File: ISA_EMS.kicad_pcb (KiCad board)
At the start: 2 copper layers, 176.5 x 102.9 mm, 57 parts, among them J1 ISA BUS, J2 EMS Address, J3 ROM Config, U1 74HCT688, U10 74HCT32, U11 74HCT04, U12 74ACT245, U13 AS6C4008-55PCN, U14 AS6C4008-55PCN, U15 AS6C4008-55PCN, U16 AS6C4008-55PCN, U17 74HCT138, U18 74LS573, U19 74LS573, U2 SST39SF040, U20 74LS573, U21 74LS573, U3 AS6C4008-55PCN, U4 AS6C4008-55PCN, U5 AS6C4008-55PCN, U6 AS6C4008-55PCN, U7 74HCT688, U8 74HCT688, U9 74HCT139

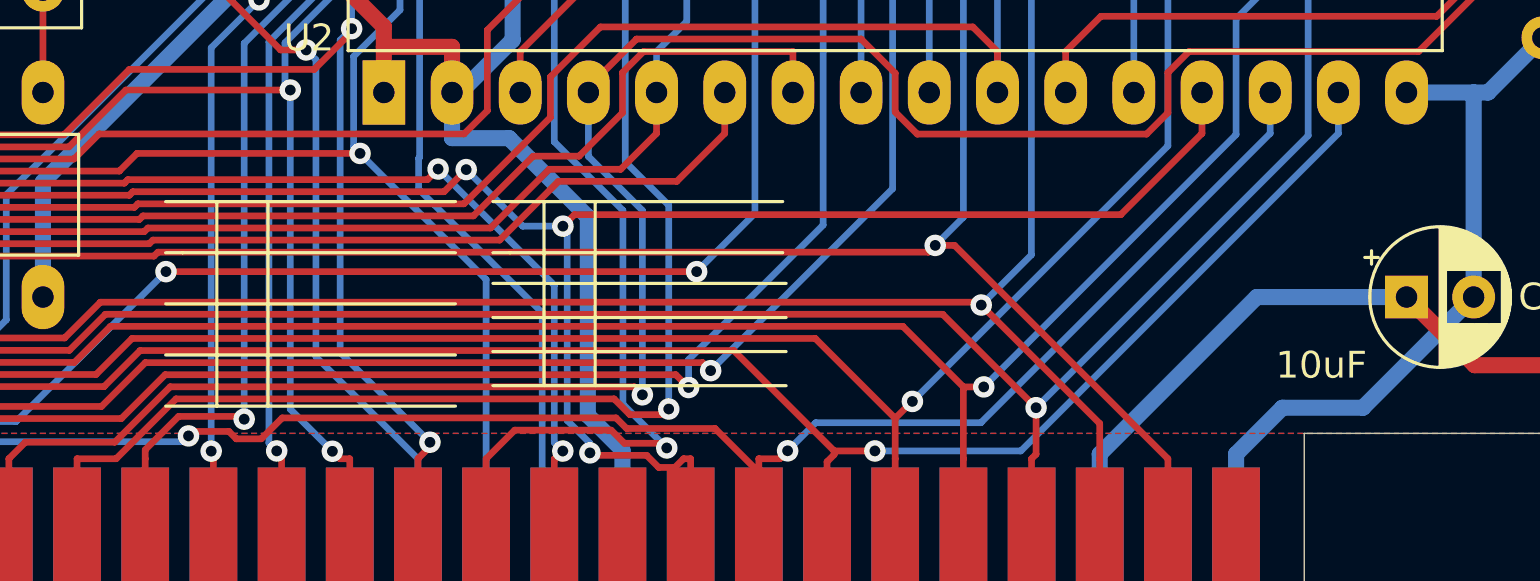
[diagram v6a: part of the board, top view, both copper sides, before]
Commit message: Updated silkscreen
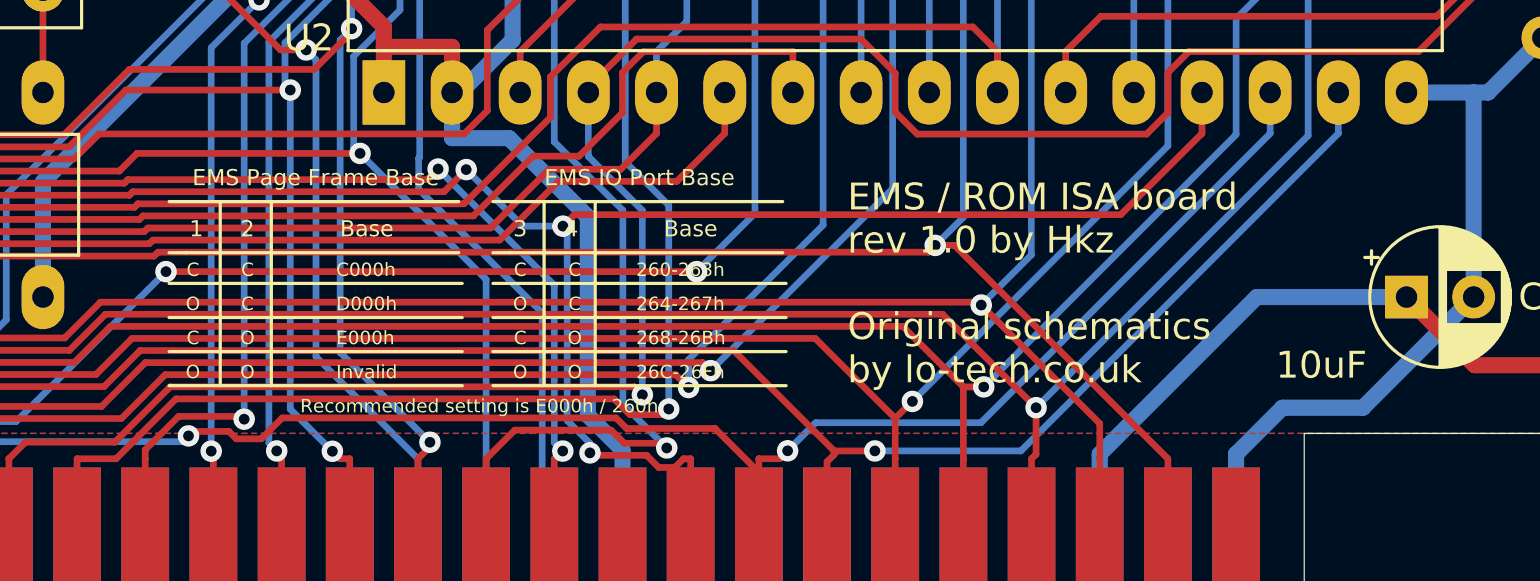
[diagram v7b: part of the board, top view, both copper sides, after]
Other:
- board text added: "260-263h"
- board text added: "264-267h"
- board text added: "268-26Bh"
- board text added: "26C-26Fh"
- board text added: "Base"
- board text added: "C"
- board text added: "C000h"
- board text added: "D000h"
- board text added: "E000h"
- board text added: "EMS / ROM ISA board rev 1.0 by Hkz Original schematics by lo-tech.co.uk"
- board text added: "EMS IO Port Base"
- board text added: "EMS Page Frame Base"
- board text added: "Invalid"
- board text added: "O"
- board text added: "Recommended setting is E000h / 260h"
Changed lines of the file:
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@@
   (general
     (thickness 1.6)
-    (drawings 92)
+    (drawings 127)
     (tracks 3500)
     (zones 0)
@@
     )
   )
+  (gr_text "EMS / ROM ISA board\nrev 1.0 by Hkz\n\nOriginal schematics \nby lo-tech.co.uk" (at 275.082 188.722) (layer F.SilkS)
+    (effects (font (size 1 1) (thickness 0.25)) (justify left))
+  )
+  (gr_text "Recommended setting is E000h / 260h" (at 261.366 193.294) (layer F.SilkS)
+    (effects (font (size 0.5 0.5) (thickness 0.125)))
+  )
+  (gr_text 26C-26Fh (at 267.208 192.024) (layer F.SilkS)
+    (effects (font (size 0.5 0.5) (thickness 0.125)) (justify left))
+  )
+  (gr_text 268-26Bh (at 267.208 190.754) (layer F.SilkS)
+    (effects (font (size 0.5 0.5) (thickness 0.125)) (justify left))
+  )
+  (gr_text 264-267h (at 267.208 189.484) (layer F.SilkS)
+    (effects (font (size 0.5 0.5) (thickness 0.125)) (justify left))
+  )
+  (gr_text 260-263h (at 267.208 188.214) (layer F.SilkS)
+    (effects (font (size 0.5 0.5) (thickness 0.125)) (justify left))
+  )
+  (gr_text O (at 264.922 192.024) (layer F.SilkS)
+    (effects (font (size 0.5 0.5) (thickness 0.125)))
+  )
+  (gr_text C (at 264.922 188.214) (layer F.SilkS)
+    (effects (font (size 0.5 0.5) (thickness 0.125)))
+  )
+  (gr_text C (at 264.922 189.484) (layer F.SilkS)
+    (effects (font (size 0.5 0.5) (thickness 0.125)))
+  )
+  (gr_text C (at 262.89 190.754) (layer F.SilkS)
+    (effects (font (size 0.5 0.5) (thickness 0.125)))
+  )
+  (gr_text O (at 262.89 189.484) (layer F.SilkS)
+    (effects (font (size 0.5 0.5) (thickness 0.125)))
+  )
+  (gr_text O (at 262.89 192.024) (layer F.SilkS)
+    (effects (font (size 0.5 0.5) (thickness 0.125)))
+  )
+  (gr_text O (at 264.922 190.754) (layer F.SilkS)
+    (effects (font (size 0.5 0.5) (thickness 0.125)))
+  )
+  (gr_text C (at 262.89 188.214) (layer F.SilkS)
+    (effects (font (size 0.5 0.5) (thickness 0.125)))
+  )
+  (gr_text C000h (at 256.032 188.214) (layer F.SilkS)
+    (effects (font (size 0.5 0.5) (thickness 0.125)) (justify left))
+  )
+  (gr_text D000h (at 256.032 189.484) (layer F.SilkS)
+    (effects (font (size 0.5 0.5) (thickness 0.125)) (justify left))
+  )
+  (gr_text E000h (at 256.032 190.754) (layer F.SilkS)
+    (effects (font (size 0.5 0.5) (thickness 0.125)) (justify left))
+  )
+  (gr_text Invalid (at 256.032 192.024) (layer F.SilkS)
+    (effects (font (size 0.5 0.5) (thickness 0.125)) (justify left))
+  )
+  (gr_text O (at 252.73 192.024) (layer F.SilkS)
+    (effects (font (size 0.5 0.5) (thickness 0.125)))
+  )
+  (gr_text O (at 250.698 192.024) (layer F.SilkS)
+    (effects (font (size 0.5 0.5) (thickness 0.125)))
+  )
+  (gr_text C (at 250.698 190.754) (layer F.SilkS)
+    (effects (font (size 0.5 0.5) (thickness 0.125)))
+  )
+  (gr_text O (at 252.73 190.754) (layer F.SilkS)
+    (effects (font (size 0.5 0.5) (thickness 0.125)))
+  )
+  (gr_text C (at 252.73 189.484) (layer F.SilkS)
+    (effects (font (size 0.5 0.5) (thickness 0.125)))
+  )
+  (gr_text O (at 250.698 189.484) (layer F.SilkS)
+    (effects (font (size 0.5 0.5) (thickness 0.125)))
+  )
+  (gr_text C (at 252.73 188.214) (layer F.SilkS)
+    (effects (font (size 0.5 0.5) (thickness 0.125)))
+  )
+  (gr_text C (at 250.698 188.214) (layer F.SilkS)
+    (effects (font (size 0.5 0.5) (thickness 0.125)))
+  )
+  (gr_text Base (at 269.24 186.69) (layer F.SilkS)
+    (effects (font (size 0.6 0.6) (thickness 0.15)))
+  )
+  (gr_text Base (at 257.175 186.69) (layer F.SilkS)
+    (effects (font (size 0.6 0.6) (thickness 0.15)))
+  )
+  (gr_text 4 (at 264.795 186.69) (layer F.SilkS)
+    (effects (font (size 0.6 0.6) (thickness 0.15)))
+  )
+  (gr_text 3 (at 262.89 186.69) (layer F.SilkS)
+    (effects (font (size 0.6 0.6) (thickness 0.15)))
+  )
+  (gr_text 2 (at 252.73 186.69) (layer F.SilkS)
+    (effects (font (size 0.6 0.6) (thickness 0.15)))
+  )
+  (gr_text 1 (at 250.825 186.69) (layer F.SilkS)
+    (effects (font (size 0.6 0.6) (thickness 0.15)))
+  )
+  (gr_text "EMS IO Port Base" (at 267.335 184.785) (layer F.SilkS)
+    (effects (font (size 0.6 0.6) (thickness 0.15)))
+  )
+  (gr_text "EMS Page Frame Base" (at 255.27 184.785) (layer F.SilkS)
+    (effects (font (size 0.6 0.6) (thickness 0.15)))
+  )
+  (gr_line (start 250.444 185.674) (end 260.604 185.674) (layer F.SilkS) (width 0.12))
+  (gr_line (start 250.444 185.674) (end 249.809 185.674) (layer F.SilkS) (width 0.12))
+  (gr_line (start 250.444 187.579) (end 249.809 187.579) (layer F.SilkS) (width 0.12))
+  (gr_line (start 250.444 187.579) (end 260.604 187.579) (layer F.SilkS) (width 0.12))
+  (gr_line (start 253.619 187.579) (end 253.619 192.532) (layer F.SilkS) (width 0.12))
+  (gr_line (start 251.714 187.579) (end 251.714 192.532) (layer F.SilkS) (width 0.12))
+  (gr_line (start 249.809 188.722) (end 260.731 188.722) (layer F.SilkS) (width 0.12))
+  (gr_line (start 253.619 185.674) (end 253.619 187.579) (layer F.SilkS) (width 0.12))
+  (gr_line (start 251.714 185.674) (end 251.714 187.579) (layer F.SilkS) (width 0.12))
+  (gr_line (start 249.809 191.262) (end 260.731 191.262) (layer F.SilkS) (width 0.12))
+  (gr_line (start 249.809 192.532) (end 260.731 192.532) (layer F.SilkS) (width 0.12))
+  (gr_line (start 249.809 189.992) (end 260.731 189.992) (layer F.SilkS) (width 0.12))
   (gr_text A15 (at 298.45 163.195 90) (layer F.SilkS)
     (effects (font (size 1 1) (thickness 0.25)))
@@
   (gr_line (start 262.509 185.674) (end 272.669 185.674) (layer F.SilkS) (width 0.12))
   (gr_line (start 263.779 187.579) (end 263.779 192.532) (layer F.SilkS) (width 0.12))
-  (gr_line (start 251.587 187.579) (end 251.587 193.294) (layer F.SilkS) (width 0.12))
-  (gr_line (start 253.492 187.579) (end 253.492 193.294) (layer F.SilkS) (width 0.12))
-  (gr_line (start 249.682 193.294) (end 260.477 193.294) (layer F.SilkS) (width 0.12))
-  (gr_line (start 249.682 191.389) (end 260.477 191.389) (layer F.SilkS) (width 0.12))
-  (gr_line (start 249.682 189.484) (end 260.477 189.484) (layer F.SilkS) (width 0.12))
-  (gr_line (start 253.492 185.674) (end 253.492 187.579) (layer F.SilkS) (width 0.12))
-  (gr_line (start 250.317 187.579) (end 249.682 187.579) (layer F.SilkS) (width 0.12))
-  (gr_line (start 250.317 185.674) (end 249.682 185.674) (layer F.SilkS) (width 0.12))
-  (gr_line (start 251.587 185.674) (end 251.587 187.579) (layer F.SilkS) (width 0.12))
-  (gr_line (start 250.317 187.579) (end 260.477 187.579) (layer F.SilkS) (width 0.12))
-  (gr_line (start 250.317 185.674) (end 260.477 185.674) (layer F.SilkS) (width 0.12))
   (dimension 56.515 (width 0.15) (layer Dwgs.User)
     (gr_text "56,515 mm" (at 328.833 162.8775 90) (layer Dwgs.User)

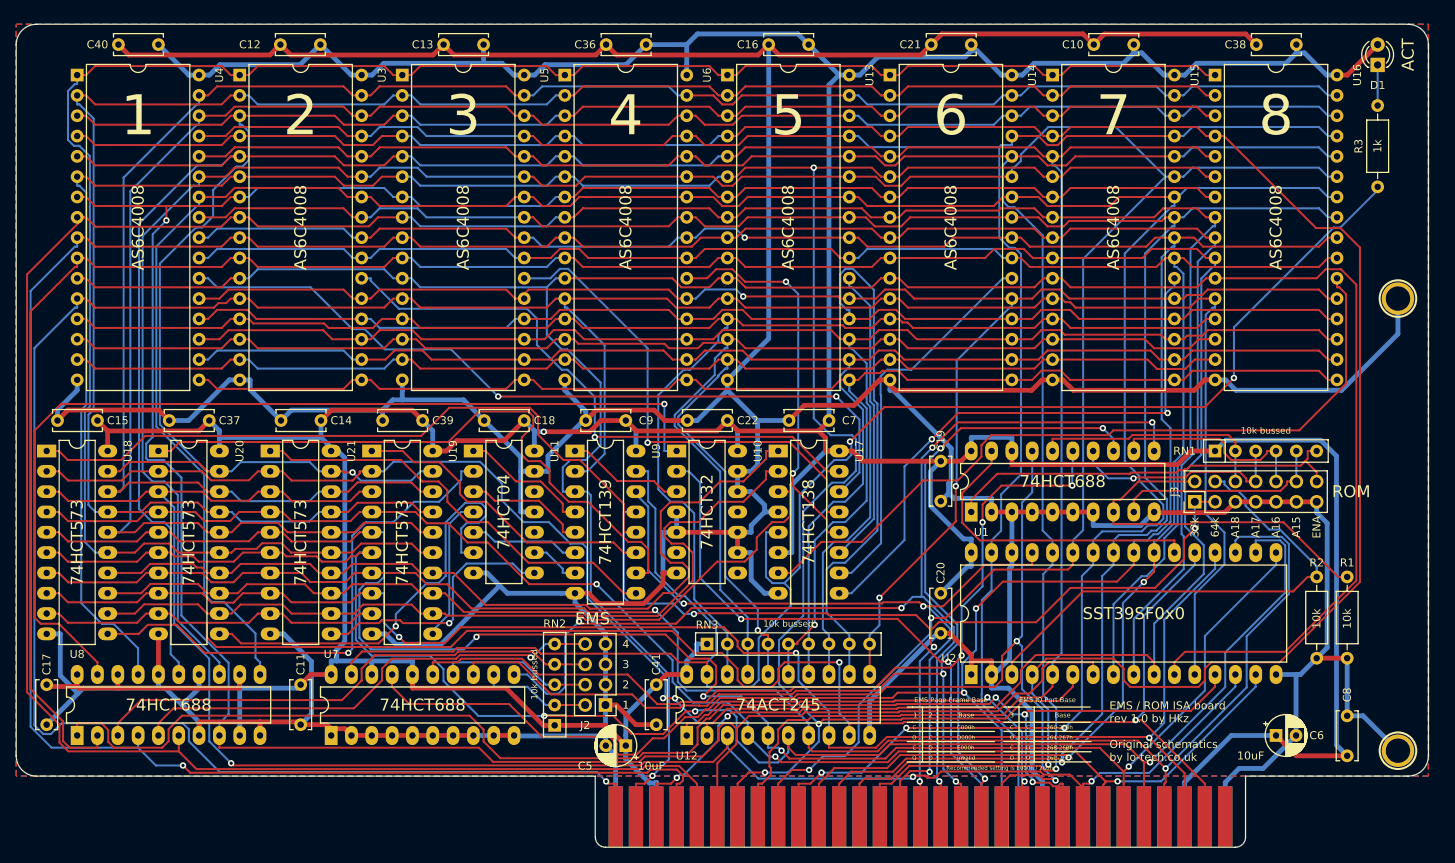
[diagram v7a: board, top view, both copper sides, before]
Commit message: Removed BOOTROM, make board smaller, reroute
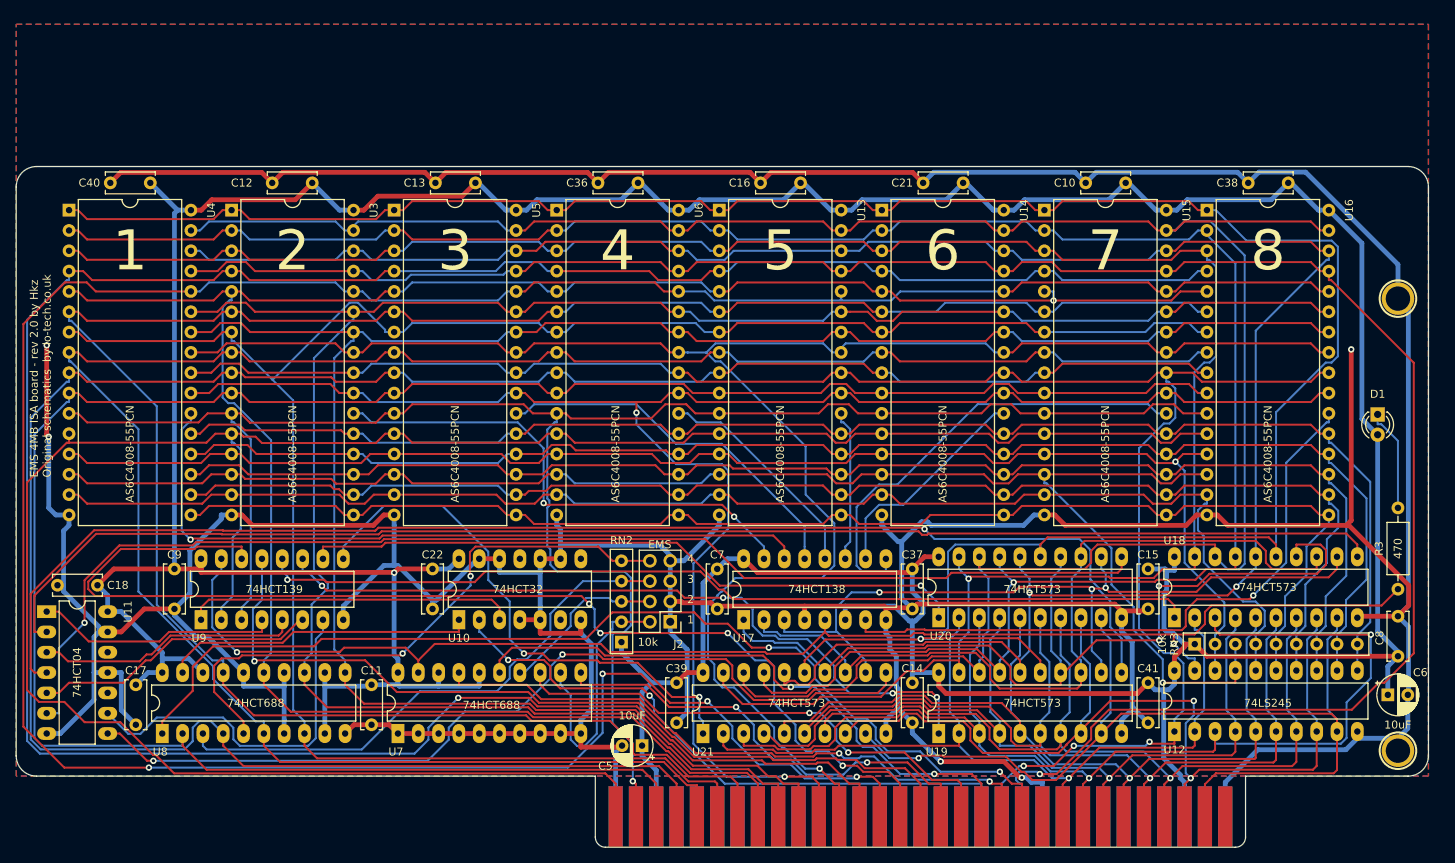
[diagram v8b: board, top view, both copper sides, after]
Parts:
- removed C19, C20: 100nF, Capacitor_THT:C_Disc_D6.0mm_W2.5mm_P5.00mm
- removed J3: ROM Config, Connector_PinHeader_2.54mm:PinHeader_2x07_P2.54mm_Vertical
- removed R1, R2: 10k, Resistor_THT:R_Axial_DIN0207_L6.3mm_D2.5mm_P10.16mm_Horizontal
- removed RN1: 10k, Resistor_THT:R_Array_SIP6
- removed U1: 74HCT688, Package_DIP:DIP-20_W7.62mm_LongPads
- removed U2: SST39SF040, Package_DIP:DIP-32_W15.24mm_LongPads
- R3: value 1k -> 470
- U12: value 74ACT245 -> 74LS245
- U18, U19, U20, U21: value 74LS573 -> 74HCT573
- moved U18 142.5 mm to (283.2, 174.5), turned to 90 degrees
- moved C15 132.6 mm to (279.9, 168.4), turned to 270 degrees
- moved U20 99.7 mm to (253.7, 174.5), turned to 90 degrees
- moved C37 89.8 mm to (250.4, 168.4), turned to 270 degrees
- moved C14 80.9 mm to (250.4, 182.6), turned to 270 degrees
- moved U19 79.2 mm to (253.7, 189.0), turned to 90 degrees
- moved U21 64.6 mm to (224.3, 189.0), turned to 90 degrees
- moved C41 61.5 mm to (279.9, 182.6)
- moved U12 61.0 mm to (283.2, 188.7)
- moved RN3 61.0 mm to (285.8, 177.8)
- moved C9 59.4 mm to (158.2, 168.4), turned to 270 degrees
- moved C18 57.2 mm to (148.6, 170.4)
- moved U11 57.0 mm to (142.2, 173.7)
- moved U9 51.3 mm to (161.5, 174.8), turned to 90 degrees
- moved R3 50.4 mm to (311.1, 170.9)
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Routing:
- net /REG1-LOAD: track 18.2 -> 165.6 mm, vias 0 -> 1
- net /REG0-LOAD: track 65.9 -> 177.2 mm, vias 1 -> 0
- net /D4: track 219.2 -> 109.2 mm, vias 3 -> 1
- net /D3: track 212.7 -> 107.0 mm, vias 4 -> 1
- net /A4: track 370.6 -> 268.9 mm
- net /REG2-LOAD: track 55.4 -> 155.3 mm
- net /D5: track 208.9 -> 109.6 mm, vias 2 -> 1
- net /D7: track 218.9 -> 123.7 mm, vias 2 -> 1
- net /A13: track 257.4 -> 352.3 mm, vias 1 -> 4
- net /A5: track 354.4 -> 261.7 mm, vias 1 -> 0
- net /D0: track 195.4 -> 105.3 mm, vias 5 -> 1
- net /A16: track 143.0 -> 58.1 mm, vias 5 -> 2
- net Net-(U10-Pad1): track 122.6 -> 39.1 mm, vias 1 -> 0
- net VCC: track 681.1 -> 600.8 mm
- net /D6: track 196.2 -> 117.5 mm, vias 3 -> 2
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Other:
- board size 176.5 x 102.9 mm -> 176.5 x 85.1 mm
- board text added: "EMS 4MB ISA board - rev 2.0 by Hkz Original schematics by lo-tech.co.uk"
- board text removed: "10k"
- board text removed: "10k bussed"
- board text removed: "10uF"
- board text removed: "1k"
- board text removed: "32k"
- board text removed: "64k"
- board text removed: "74ACT245"
- board text removed: "74HCT04"
- board text removed: "74HCT138"
- board text removed: "74HCT139"
- board text removed: "74HCT32"
- board text removed: "74HCT573"
- board text removed: "74HCT688"
- board text removed: "A15"
- board text removed: "A16"
- board text removed: "A17"
- board text removed: "A18"
- board text removed: "ACT"
- board text removed: "AS6C4008"
- board text removed: "EMS / ROM ISA board rev 1.0 by Hkz Original schematics by lo-tech.co.uk"
- board text removed: "ENA"
- board text removed: "ROM"
- board text removed: "SST39SF0x0"
